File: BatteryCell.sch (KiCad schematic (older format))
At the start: 9 parts

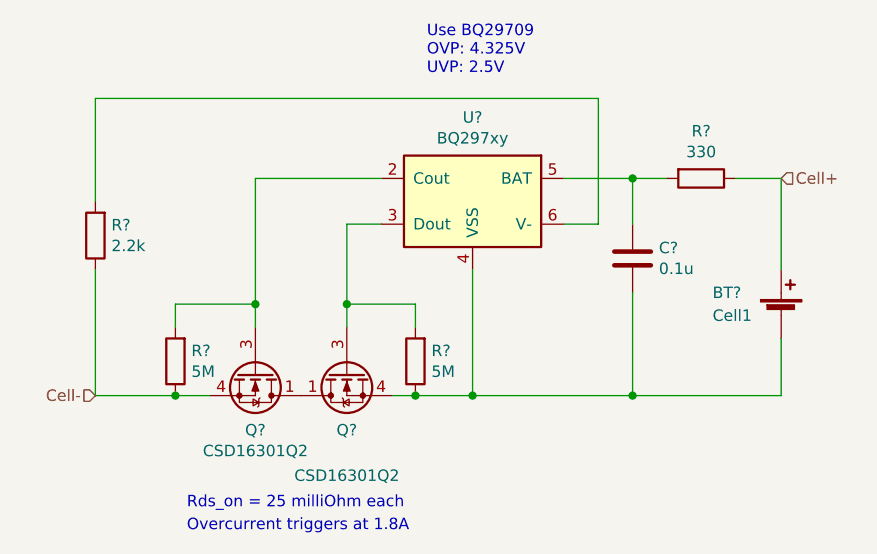
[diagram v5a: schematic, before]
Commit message: changed mosfets in inhibit
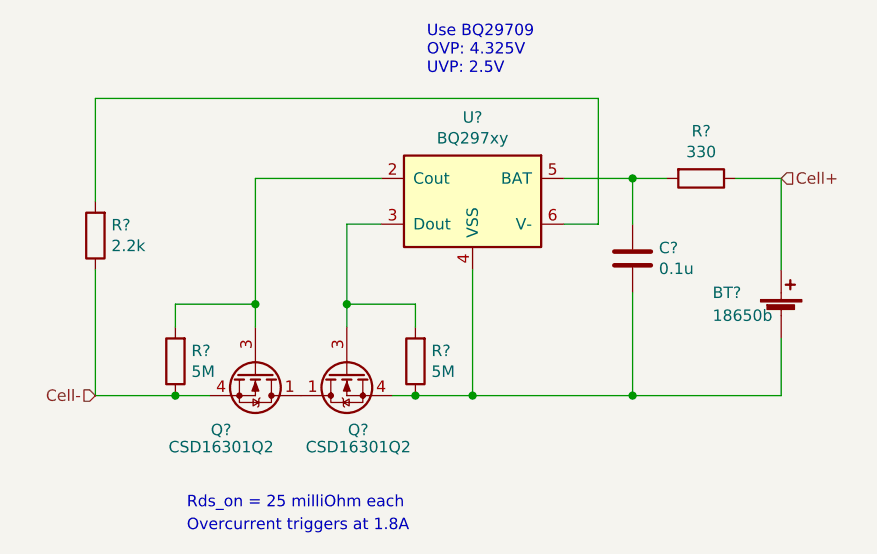
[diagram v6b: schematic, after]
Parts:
- BT?: value Cell1 -> 18650b
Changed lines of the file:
@@
 $Descr A4 11693 8268
 encoding utf-8
-Sheet 2 14
+Sheet 3 14
 Title ""
 Date ""
@@
 AR Path="/5D0BC9BA/5D087B3A" Ref="BT?"  Part="1"
 F 0 "BT?" H 6750 4200 50  0000 L CNN
-F 1 "Cell1" H 6750 4100 50  0000 L CNN
+F 1 "18650b" H 6750 4100 50  0000 L CNN
 F 2 "" V 7050 4160 50  0001 C CNN
 F 3 "~" V 7050 4160 50  0001 C CNN
@@
 AR Path="/5D0B1FBC/5D0458C0" Ref="Q?"  Part="1"
 AR Path="/5D0BC9BA/5D0458C0" Ref="Q?"  Part="1"
-F 0 "Q?" V 5001 4350 50  0000 C CNN
-F 1 "CSD16301Q2" V 5092 4350 50  0000 C CNN
+F 0 "Q?" V 5000 4200 50  0000 C CNN
+F 1 "CSD16301Q2" V 5075 4200 50  0000 C CNN
 F 2 "Package_SON:Texas_DQK" H 4950 4275 50  0001 L CIN
 F 3 "http://www.ti.com/lit/ds/symlink/csd16301q2.pdf" V 4750 4350 50  0001 L CNN
@@
 AR Path="/5D0B1FBC/5D04731F" Ref="Q?"  Part="1"
 AR Path="/5D0BC9BA/5D04731F" Ref="Q?"  Part="1"
-F 0 "Q?" V 5401 4350 50  0000 C CNN
-F 1 "CSD16301Q2" V 5600 4350 50  0000 C CNN
+F 0 "Q?" V 5400 4300 50  0000 C CNN
+F 1 "CSD16301Q2" V 5475 4300 50  0000 C CNN
 F 2 "Package_SON:Texas_DQK" H 5350 4275 50  0001 L CIN
 F 3 "http://www.ti.com/lit/ds/symlink/csd16301q2.pdf" V 5150 4350 50  0001 L CNN

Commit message: added burn wire load switches
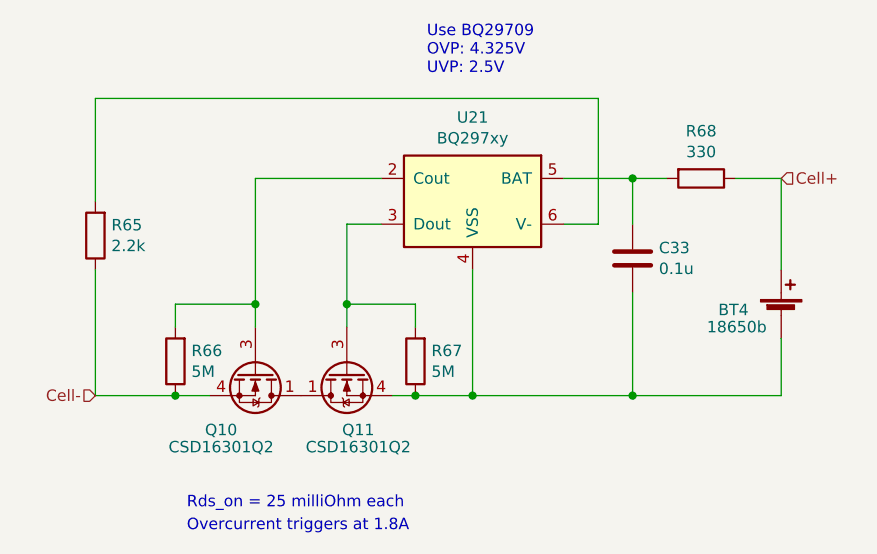
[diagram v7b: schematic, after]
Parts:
- gave numbers to parts that had none: 9
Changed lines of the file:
@@
 $Descr A4 11693 8268
 encoding utf-8
-Sheet 3 14
+Sheet 5 14
 Title ""
 Date ""
@@
 P 7050 4100
 AR Path="/5D087B3A" Ref="BT?"  Part="1"
-AR Path="/5D07F3FC/5D087B3A" Ref="BT?"  Part="1"
-AR Path="/5D0A75A0/5D087B3A" Ref="BT?"  Part="1"
-AR Path="/5D0B1FBC/5D087B3A" Ref="BT?"  Part="1"
-AR Path="/5D0BC9BA/5D087B3A" Ref="BT?"  Part="1"
-F 0 "BT?" H 6750 4200 50  0000 L CNN
-F 1 "18650b" H 6750 4100 50  0000 L CNN
+AR Path="/5D07F3FC/5D087B3A" Ref="BT1"  Part="1"
+AR Path="/5D0A75A0/5D087B3A" Ref="BT2"  Part="1"
+AR Path="/5D0B1FBC/5D087B3A" Ref="BT3"  Part="1"
+AR Path="/5D0BC9BA/5D087B3A" Ref="BT4"  Part="1"
+F 0 "BT4" H 6775 4125 50  0000 L CNN
+F 1 "18650b" H 6725 4050 50  0000 L CNN
 F 2 "" V 7050 4160 50  0001 C CNN
 F 3 "~" V 7050 4160 50  0001 C CNN
@@
 P 5700 3600
 AR Path="/5D087B48" Ref="U?"  Part="1"
-AR Path="/5D07F3FC/5D087B48" Ref="U?"  Part="1"
-AR Path="/5D0A75A0/5D087B48" Ref="U?"  Part="1"
-AR Path="/5D0B1FBC/5D087B48" Ref="U?"  Part="1"
-AR Path="/5D0BC9BA/5D087B48" Ref="U?"  Part="1"
-F 0 "U?" H 5700 3967 50  0000 C CNN
+AR Path="/5D07F3FC/5D087B48" Ref="U18"  Part="1"
+AR Path="/5D0A75A0/5D087B48" Ref="U19"  Part="1"
+AR Path="/5D0B1FBC/5D087B48" Ref="U20"  Part="1"
+AR Path="/5D0BC9BA/5D087B48" Ref="U21"  Part="1"
+F 0 "U21" H 5700 3967 50  0000 C CNN
 F 1 "BQ297xy" H 5700 3876 50  0000 C CNN
 F 2 "Package_SON:WSON-6_1.5x1.5mm_P0.5mm" H 5700 3950 50  0001 C CNN
@@
 P 6700 3500
 AR Path="/5D087B60" Ref="R?"  Part="1"
-AR Path="/5D07F3FC/5D087B60" Ref="R?"  Part="1"
-AR Path="/5D0A75A0/5D087B60" Ref="R?"  Part="1"
-AR Path="/5D0B1FBC/5D087B60" Ref="R?"  Part="1"
-AR Path="/5D0BC9BA/5D087B60" Ref="R?"  Part="1"
-F 0 "R?" V 6493 3500 50  0000 C CNN
+AR Path="/5D07F3FC/5D087B60" Ref="R56"  Part="1"
+AR Path="/5D0A75A0/5D087B60" Ref="R60"  Part="1"
+AR Path="/5D0B1FBC/5D087B60" Ref="R64"  Part="1"
+AR Path="/5D0BC9BA/5D087B60" Ref="R68"  Part="1"
+F 0 "R68" V 6493 3500 50  0000 C CNN
 F 1 "330" V 6584 3500 50  0000 C CNN
 F 2 "" V 6630 3500 50  0001 C CNN
@@
 P 6400 3850
 AR Path="/5D087B69" Ref="C?"  Part="1"
-AR Path="/5D07F3FC/5D087B69" Ref="C?"  Part="1"
-AR Path="/5D0A75A0/5D087B69" Ref="C?"  Part="1"
-AR Path="/5D0B1FBC/5D087B69" Ref="C?"  Part="1"
-AR Path="/5D0BC9BA/5D087B69" Ref="C?"  Part="1"
-F 0 "C?" H 6515 3896 50  0000 L CNN
+AR Path="/5D07F3FC/5D087B69" Ref="C30"  Part="1"
+AR Path="/5D0A75A0/5D087B69" Ref="C31"  Part="1"
+AR Path="/5D0B1FBC/5D087B69" Ref="C32"  Part="1"
+AR Path="/5D0BC9BA/5D087B69" Ref="C33"  Part="1"
+F 0 "C33" H 6515 3896 50  0000 L CNN
 F 1 "0.1u" H 6515 3805 50  0000 L CNN
 F 2 "" H 6438 3700 50  0001 C CNN
@@
 P 4050 3750
 AR Path="/5D087B7B" Ref="R?"  Part="1"
-AR Path="/5D07F3FC/5D087B7B" Ref="R?"  Part="1"
-AR Path="/5D0A75A0/5D087B7B" Ref="R?"  Part="1"
-AR Path="/5D0B1FBC/5D087B7B" Ref="R?"  Part="1"
-AR Path="/5D0BC9BA/5D087B7B" Ref="R?"  Part="1"
-F 0 "R?" H 3980 3704 50  0000 R CNN
+AR Path="/5D07F3FC/5D087B7B" Ref="R53"  Part="1"
+AR Path="/5D0A75A0/5D087B7B" Ref="R57"  Part="1"
+AR Path="/5D0B1FBC/5D087B7B" Ref="R61"  Part="1"
+AR Path="/5D0BC9BA/5D087B7B" Ref="R65"  Part="1"
+F 0 "R65" H 3980 3704 50  0000 R CNN
 F 1 "2.2k" H 3980 3795 50  0000 R CNN
 F 2 "" V 3980 3750 50  0001 C CNN
@@
 P 5450 4300
 AR Path="/5CF617A0" Ref="R?"  Part="1"
-AR Path="/5D07F3FC/5CF617A0" Ref="R?"  Part="1"
-AR Path="/5D0A75A0/5CF617A0" Ref="R?"  Part="1"
-AR Path="/5D0B1FBC/5CF617A0" Ref="R?"  Part="1"
-AR Path="/5D0BC9BA/5CF617A0" Ref="R?"  Part="1"
-F 0 "R?" H 5380 4254 50  0000 R CNN
+AR Path="/5D07F3FC/5CF617A0" Ref="R55"  Part="1"
+AR Path="/5D0A75A0/5CF617A0" Ref="R59"  Part="1"
+AR Path="/5D0B1FBC/5CF617A0" Ref="R63"  Part="1"
+AR Path="/5D0BC9BA/5CF617A0" Ref="R67"  Part="1"
+F 0 "R67" H 5380 4254 50  0000 R CNN
 F 1 "5M" H 5380 4345 50  0000 R CNN
 F 2 "" V 5380 4300 50  0001 C CNN
@@
 P 4400 4300
 AR Path="/5CF6AE03" Ref="R?"  Part="1"
-AR Path="/5D07F3FC/5CF6AE03" Ref="R?"  Part="1"
-AR Path="/5D0A75A0/5CF6AE03" Ref="R?"  Part="1"
-AR Path="/5D0B1FBC/5CF6AE03" Ref="R?"  Part="1"
-AR Path="/5D0BC9BA/5CF6AE03" Ref="R?"  Part="1"
-F 0 "R?" H 4330 4254 50  0000 R CNN
+AR Path="/5D07F3FC/5CF6AE03" Ref="R54"  Part="1"
+AR Path="/5D0A75A0/5CF6AE03" Ref="R58"  Part="1"
+AR Path="/5D0B1FBC/5CF6AE03" Ref="R62"  Part="1"
+AR Path="/5D0BC9BA/5CF6AE03" Ref="R66"  Part="1"
+F 0 "R66" H 4330 4254 50  0000 R CNN
 F 1 "5M" H 4330 4345 50  0000 R CNN
 F 2 "" V 4330 4300 50  0001 C CNN
@@
 Overcurrent triggers at 1.8A
 $Comp
-L Main-rescue:CSD16301Q2-Transistor_FET Q?
+L Main-rescue:CSD16301Q2-Transistor_FET Q4
 U 1 1 5D0458C0
 P 4750 4350
-AR Path="/5D07F3FC/5D0458C0" Ref="Q?"  Part="1"
-AR Path="/5D0A75A0/5D0458C0" Ref="Q?"  Part="1"
-AR Path="/5D0B1FBC/5D0458C0" Ref="Q?"  Part="1"
-AR Path="/5D0BC9BA/5D0458C0" Ref="Q?"  Part="1"
-F 0 "Q?" V 5000 4200 50  0000 C CNN
+AR Path="/5D07F3FC/5D0458C0" Ref="Q4"  Part="1"
+AR Path="/5D0A75A0/5D0458C0" Ref="Q6"  Part="1"
+AR Path="/5D0B1FBC/5D0458C0" Ref="Q8"  Part="1"
+AR Path="/5D0BC9BA/5D0458C0" Ref="Q10"  Part="1"
+F 0 "Q10" V 5000 4200 50  0000 C CNN
 F 1 "CSD16301Q2" V 5075 4200 50  0000 C CNN
 F 2 "Package_SON:Texas_DQK" H 4950 4275 50  0001 L CIN
@@
 Connection ~ 5450 4450
 $Comp
-L Main-rescue:CSD16301Q2-Transistor_FET Q?
+L Main-rescue:CSD16301Q2-Transistor_FET Q5
 U 1 1 5D04731F
 P 5150 4350
-AR Path="/5D07F3FC/5D04731F" Ref="Q?"  Part="1"
-AR Path="/5D0A75A0/5D04731F" Ref="Q?"  Part="1"
-AR Path="/5D0B1FBC/5D04731F" Ref="Q?"  Part="1"
-AR Path="/5D0BC9BA/5D04731F" Ref="Q?"  Part="1"
-F 0 "Q?" V 5400 4300 50  0000 C CNN
+AR Path="/5D07F3FC/5D04731F" Ref="Q5"  Part="1"
+AR Path="/5D0A75A0/5D04731F" Ref="Q7"  Part="1"
+AR Path="/5D0B1FBC/5D04731F" Ref="Q9"  Part="1"
+AR Path="/5D0BC9BA/5D04731F" Ref="Q11"  Part="1"
+F 0 "Q11" V 5400 4300 50  0000 C CNN
 F 1 "CSD16301Q2" V 5475 4300 50  0000 C CNN
 F 2 "Package_SON:Texas_DQK" H 5350 4275 50  0001 L CIN
